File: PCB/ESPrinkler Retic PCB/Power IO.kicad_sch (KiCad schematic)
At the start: 33 parts, among them J1 DB910-7.62-3P-GN-S, J2 DB910-7.62-3P-GN-S, J3 DB910-7.62-3P-GN-S, J4 DB910-7.62-3P-GN-S, J5 Conn_01x04, Q1 AO3400A, Q2 AO3400A, U1 XL1509-5.0

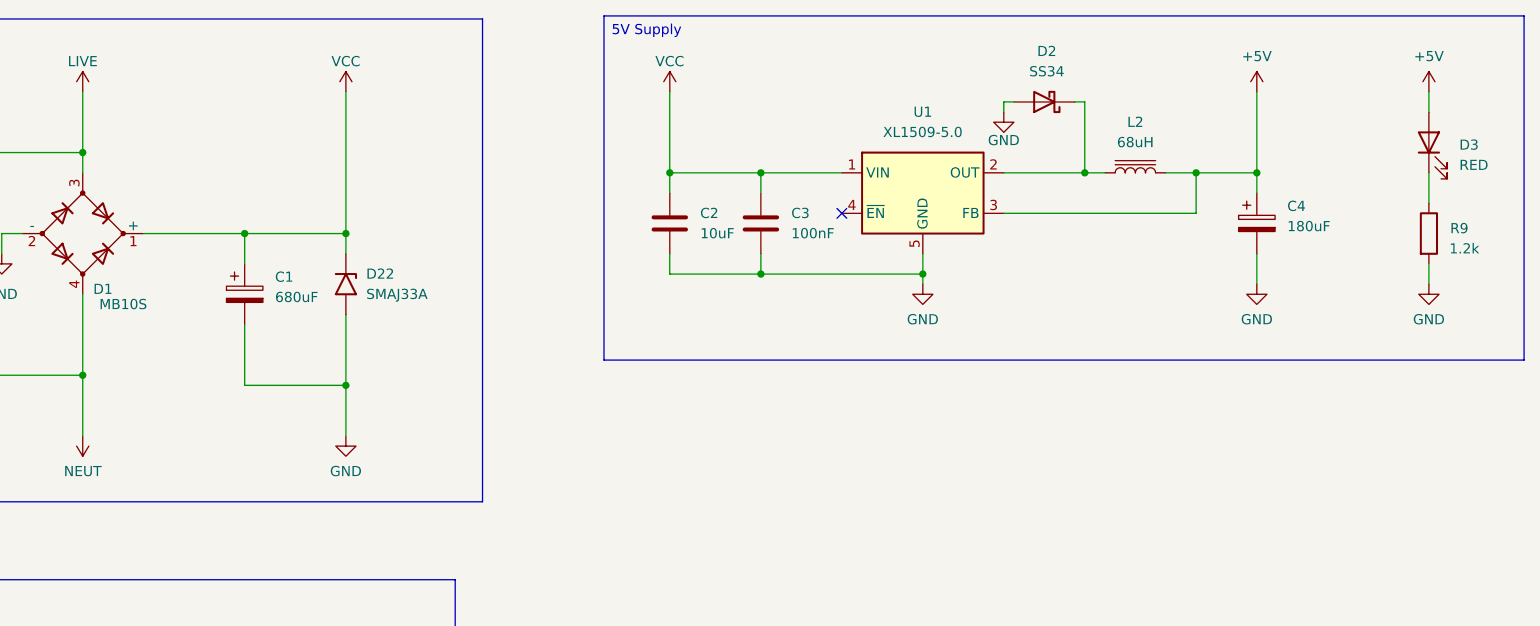
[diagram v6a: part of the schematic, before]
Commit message: Modifications after Reddit review
Changes made to design following reddit review (thank you everyone who gave their input!)

Changed rectifier reservoir cap to 470uF, added 2nd one just in case its needed.
Changed all TH caps to polymer type.
Adjusted schematic and PCB layout

Delete production files, working on new ones.
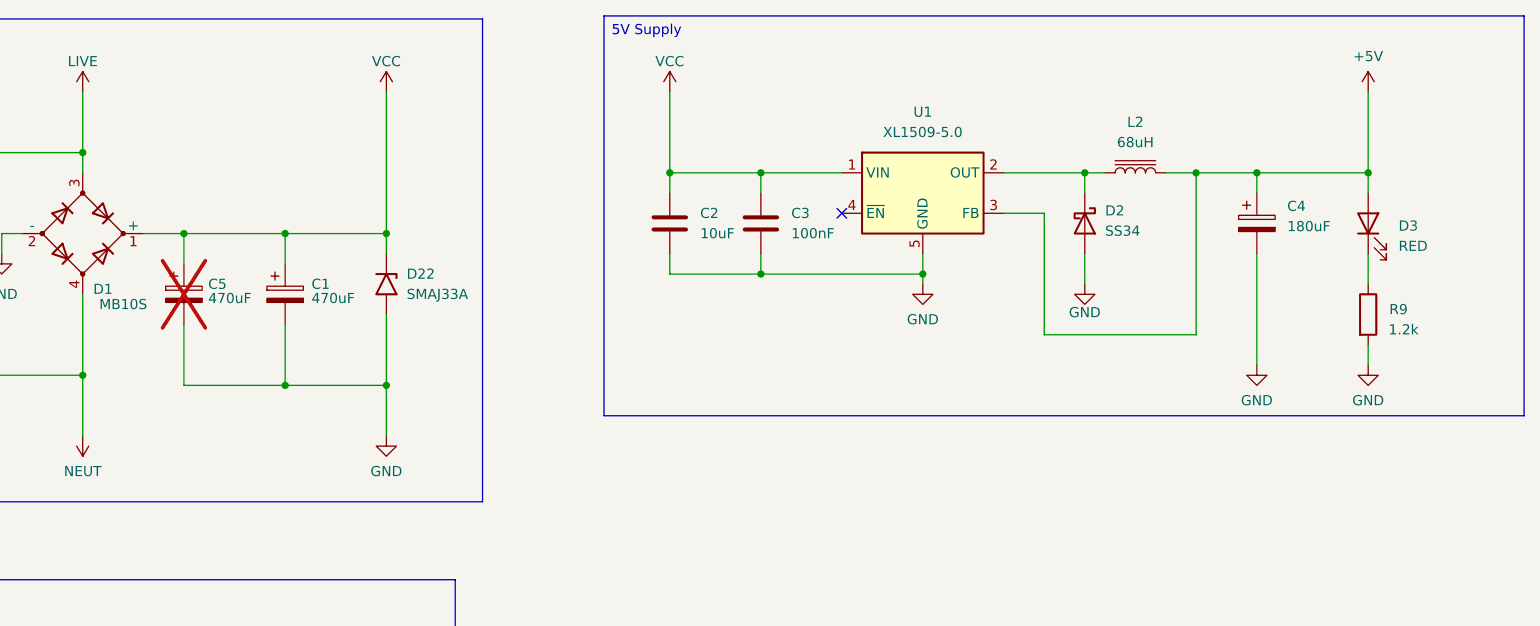
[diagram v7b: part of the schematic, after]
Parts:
- added C5: 470uF, Capacitor_THT:CP_Radial_D10.0mm_P5.00mm, symbol Device:C_Polarized
- C1: value 680uF -> 470uF; footprint Capacitor_THT:CP_Radial_D13.0mm_P5.00mm -> Capacitor_THT:CP_Radial_D10.0mm_P5.00mm; Manufacturer CX(Dongguan Chengxing Elec) -> JIERR; Manufacturer P/N GR687M050J20RR0VH4FP0 -> PA63V470M10X17; Supplier P/N C26225 -> C49232909
- C4: Manufacturer Ymin -> JIERR; Manufacturer P/N LKMC0901E181MF -> PA25V180M6X7; Supplier P/N C442817 -> C49233043
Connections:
- net GND: now also C5.2
- net VCC: now also C5.1
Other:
- moved on the sheet: C1, D2, D22, D3, R9
